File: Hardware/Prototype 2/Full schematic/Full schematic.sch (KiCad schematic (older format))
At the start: 329 parts, among them J1 Conn_01x02_Male, J10 Conn_01x01_Male, J2 Reset, J3 Encoder, J4 Failure LED, J5 Bluetooth, J6 Conn_01x02_Male, J7 Display, J8 Buttons, J9 Conn_01x02_Male, K1 EDR101A0500, K2 EDR101A0500, K3 EDR101A0500, K4 EDR101A0500, K5 EDR101A0500, K6 EDR101A0500, Q1 BC847, Q10 IRLML6402, Q11 BC847, Q12 IRFZ44, Q13 BC847, Q14 BSS138, Q15 BC847, Q16 IRF610, Q17 BC847, Q18 IRLML6402, Q19 BC847, Q2 BC847, Q20 BFS17, Q21 IRLML6402, Q22 AFT05MS003N, Q23 IRLML2502, Q24 IRLML2502, Q25 IRLML2502, Q26 IRLML2502, Q27 IRLML2502, Q28 IRLML2502, Q3 BC847, Q4 BC847, Q5 BC847, Q6 IRLML6402, Q7 IRF4905, Q8 IRLML6402, Q9 IRLML6402, U1 74LVC2T45DC, U10 ICS501, U11 STM32F103C8Tx, U12 CAT24C256, U2 74LVC2T45DC, U3 AD9835, U4 LM27313XMF, U5 LM2734X, U6 LM2734X, U7 LM2734X, U8 UC3843_SOIC8, U9 AD5245BRJZ10, X1 50MHz, Y1 8MHz, Y2 32768Hz

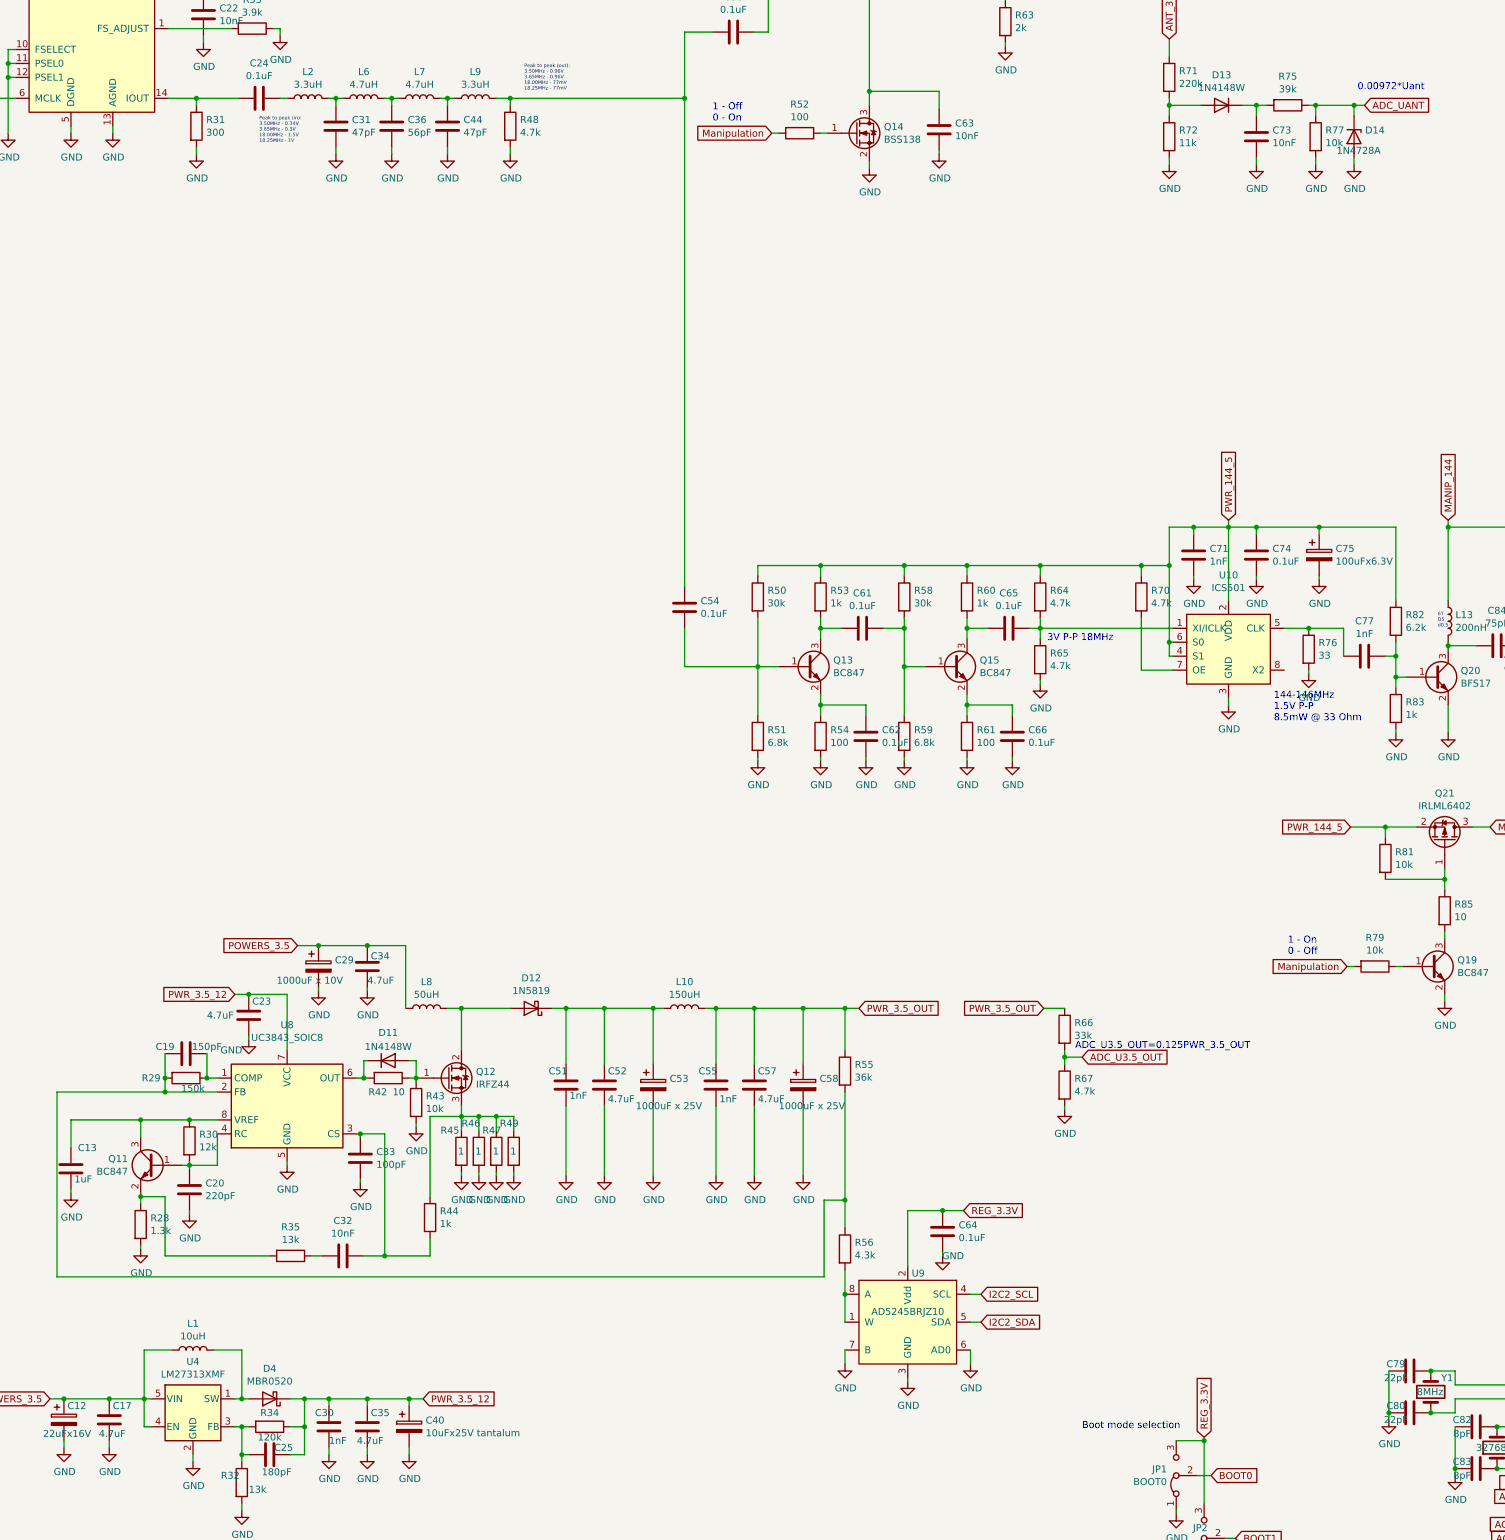
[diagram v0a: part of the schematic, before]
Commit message: Assigned cases to parts, ready to trace PCB
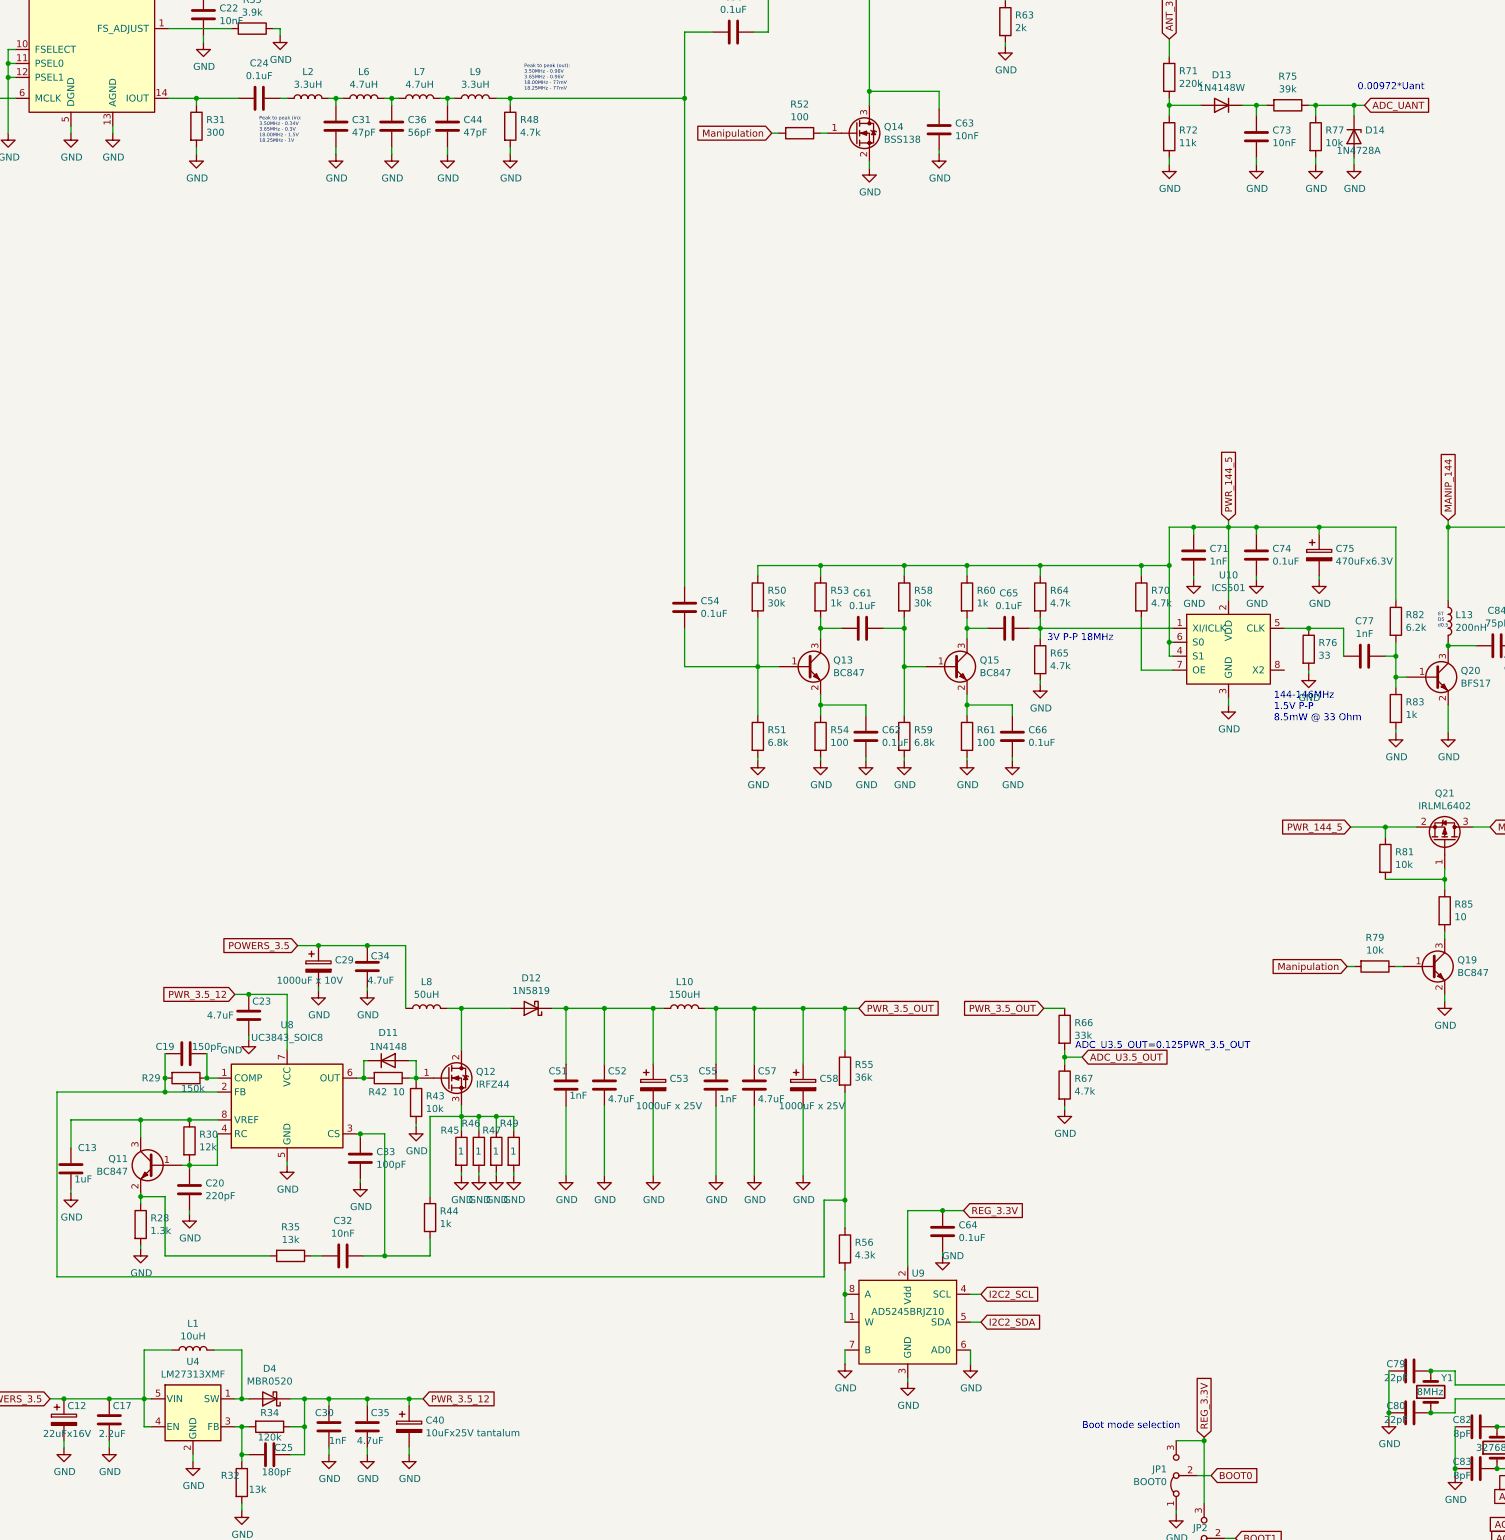
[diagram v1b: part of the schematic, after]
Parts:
- C1, C48, C49, C50: footprint Capacitor_THT:CP_Radial_D6.3mm_P2.50mm -> (none)
- C10, C11, C12, C9: footprint Capacitor_THT:CP_Radial_D4.0mm_P2.00mm -> (none)
- C100, C108, C109, C13, C14, C15, C16, C19, C20, C23, C25, C26, C27, C28, C30, C32, C33, C34, C35, C37, C38, C39, C41, C42, C43, C45, C46, C47, C51, C52, C55, C57, C6, C60, C64, C67, C70, C76, C78, C79, C80, C81, C82, C83, C85, C86, C93, C94, C95, C98: footprint Capacitor_SMD:C_0805_2012Metric_Pad1.18x1.45mm_HandSolder -> (none)
- C110: footprint Capacitor_THT:CP_Radial_D6.3mm_P2.50mm -> Capacitor_THT:CP_Radial_D8.0mm_P3.80mm
- C111: footprint Capacitor_THT:CP_Radial_D4.0mm_P2.00mm -> Capacitor_THT:CP_Radial_D8.0mm_P3.80mm
- C17: value 4.7uF -> 2.2uF; footprint Capacitor_SMD:C_0805_2012Metric_Pad1.18x1.45mm_HandSolder -> (none)
- C29, C53, C58: footprint Capacitor_THT:CP_Radial_D10.0mm_P5.00mm -> (none)
- C40: footprint Capacitor_Tantalum_SMD:CP_EIA-7260-38_AVX-R_Pad2.68x6.30mm_HandSolder -> (none)
- C75: value 100uFx6.3V -> 470uFx6.3V; footprint Capacitor_THT:CP_Radial_D6.3mm_P2.50mm -> Capacitor_THT:CP_Radial_D8.0mm_P3.80mm
- D11: value 1N4148W -> 1N4148; footprint Diode_SMD:D_SOD-123 -> (none)
- D12: footprint Diode_THT:D_DO-27_P5.08mm_Vertical_AnodeUp -> (none)
- D4, D5, D6, D7: footprint Diode_SMD:D_SOD-123 -> (none)
- J1, J2, J4, JP3, JP4: footprint Connector_PinHeader_2.54mm:PinHeader_1x02_P2.54mm_Vertical -> (none)
- J10: footprint Connector_PinHeader_2.54mm:PinHeader_1x01_P2.54mm_Vertical -> (none)
- J3, J5, J7: footprint Connector_PinHeader_2.54mm:PinHeader_1x04_P2.54mm_Vertical -> (none)
- J8, JP1, JP2: footprint Connector_PinHeader_2.54mm:PinHeader_1x03_P2.54mm_Vertical -> (none)
- L1, L3, L4, L5: footprint Inductor_SMD:L_1812_4532Metric_Pad1.30x3.40mm_HandSolder -> (none)
- L10: footprint Inductor_SMD:L_12x12mm_H8mm -> (none)
- L2, L6, L7, L9: footprint Inductor_SMD:L_1812_4532Metric_Pad1.30x3.40mm_HandSolder -> Inductor_THT:L_Radial_D9.5mm_P5.00mm_Fastron_07HVP
- L8: footprint Inductor_THT:L_Toroid_Vertical_L25.4mm_W14.7mm_P12.20mm_Vishay_TJ5_BigPads -> (none)
- Q12: footprint Package_TO_SOT_THT:TO-220-3_Vertical -> (none)
- R10, R11, R12, R13, R14, R15, R16, R17, R18, R19, R20, R21, R22, R23, R24, R28, R29, R30, R32, R34, R35, R36, R37, R38, R39, R4, R40, R41, R42, R43, R44, R5, R55, R56, R6, R66, R67, R68, R69, R7, R73, R74, R78, R79, R8, R80, R81, R84, R85, R86, R87, R88, R9, R90, R91, R92: footprint Resistor_SMD:R_0805_2012Metric_Pad1.20x1.40mm_HandSolder -> (none)
- R45, R46, R47, R49: footprint Resistor_THT:R_Axial_DIN0207_L6.3mm_D2.5mm_P2.54mm_Vertical -> (none)
- U1, U2: footprint Package_SO:VSSOP-8_2.3x2mm_P0.5mm -> Package_SO:SSOP-8_2.95x2.8mm_P0.65mm
- U12: footprint Package_SO:SOIC-8_5.23x5.23mm_P1.27mm -> (none)
- U9: footprint Package_TO_SOT_SMD:SOT-23-8_Handsoldering -> (none)
- Y1: footprint Crystal:Crystal_HC49-U_Vertical -> (none)
- Y2: footprint Crystal:Crystal_C26-LF_D2.1mm_L6.5mm_Horizontal_1EP_style1 -> (none)
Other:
- note removed: "1 - Off\n0 - On"
- note removed: "1 - On\n0 - Off"
